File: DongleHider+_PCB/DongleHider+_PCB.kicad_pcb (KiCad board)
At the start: 4 copper layers, 29.7 x 26.1 mm, 21 parts, among them J1 USB3_A, J4 D-4, J5 D+4, P1 USB_C_Plug, U1 CH334F, U2 USBLC6-2SC6, Y1 12MHz

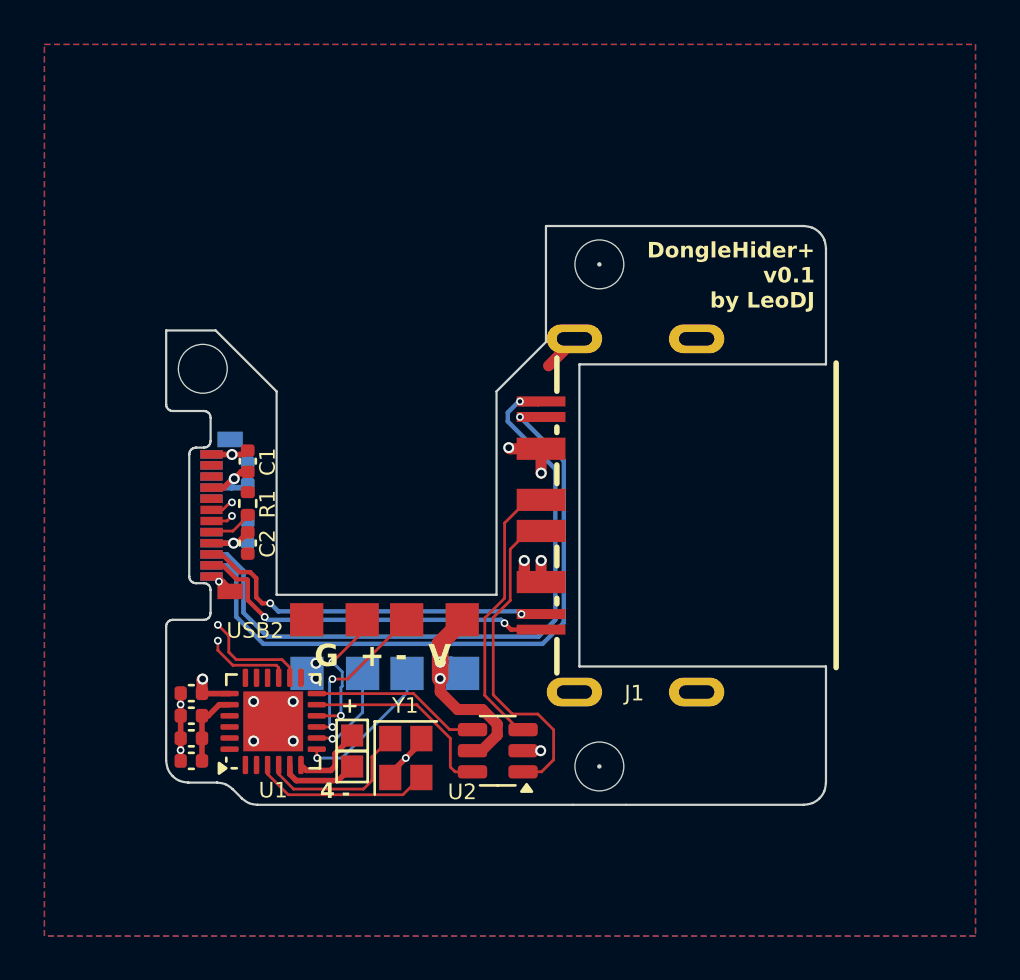
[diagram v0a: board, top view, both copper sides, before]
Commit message: final mechanical & silkscreen touches
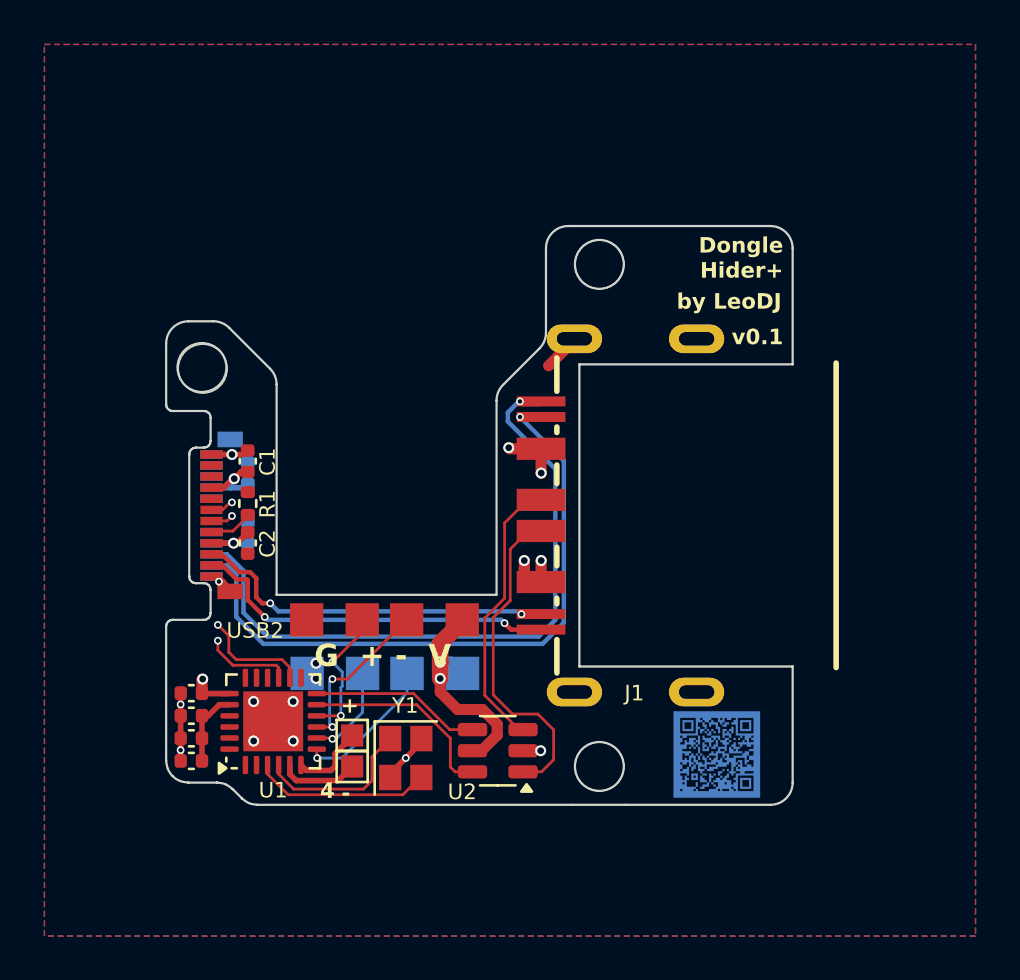
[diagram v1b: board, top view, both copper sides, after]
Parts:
- added ?: , clipboard:a3a9fe14-ccf1-44c9-aa33-5d14aabbb9b3, F.Cu at (116.3, 76.7)
- added ?: , clipboard:ed8a2803-3309-4f49-b63e-d04072c03834, B.Cu at (112.4, 76.8)
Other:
- board size 29.7 x 26.1 mm -> 28.2 x 26.1 mm
- board text added: "Dongle Hider+"
- board text added: "by LeoDJ"
- board text added: "v0.1"
- board text removed: "DongleHider+ v0.1 by LeoDJ"
